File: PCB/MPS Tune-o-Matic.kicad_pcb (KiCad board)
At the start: 2 copper layers, 83.5 x 63 mm, 82 parts, among them J1 ISP, J2 MPS, J3 USB_B_Micro, J4 12V 1A IN (5.5/2.5), J5 12V IN, Q1 PZT2222A,115, Q2 PZT2222A,115, Q3 PZT2222A,115, Q4 PZT2222A,115, Q5 PZT2222A,115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

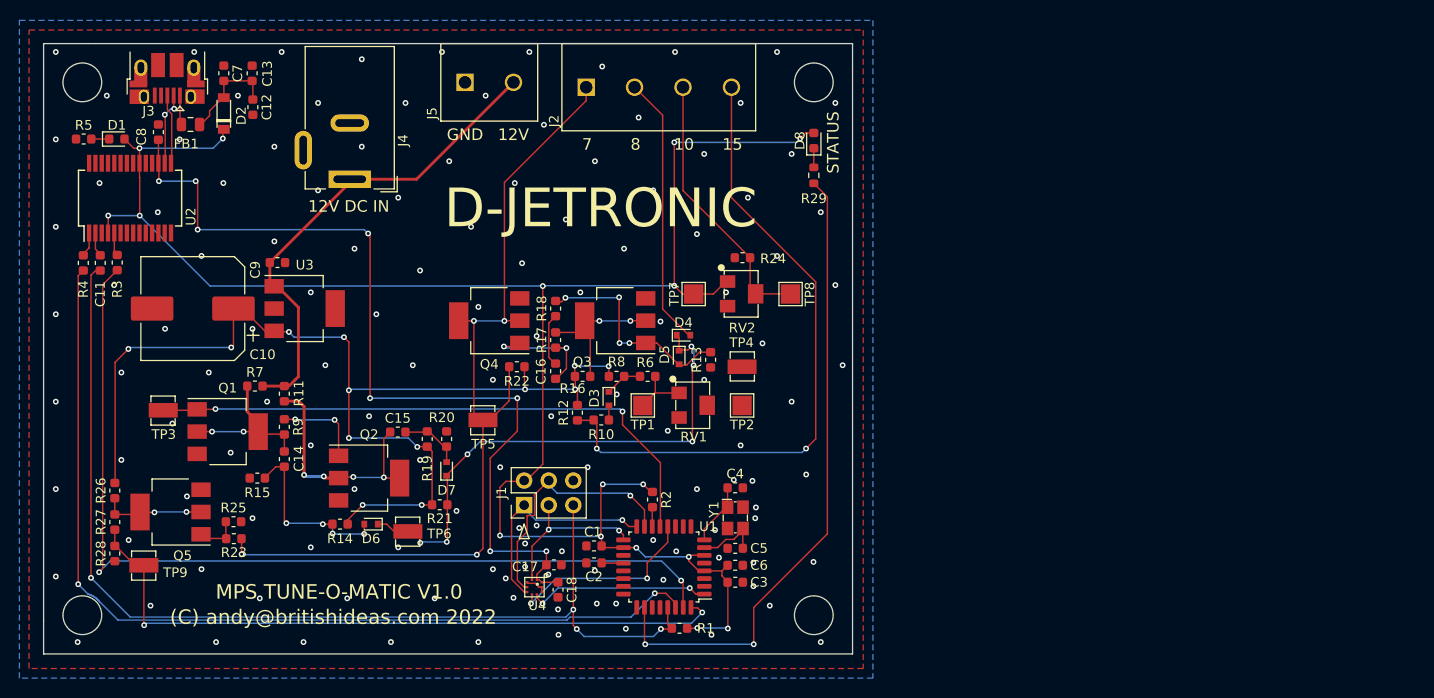
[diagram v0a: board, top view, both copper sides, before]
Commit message: Added LED for 12V power. Added resistor on MPS_STIMULUS signal. Moved track away from mounting hole. Fixed orientation of diodes. Added PDF of schematic. Updated manufacturing files.
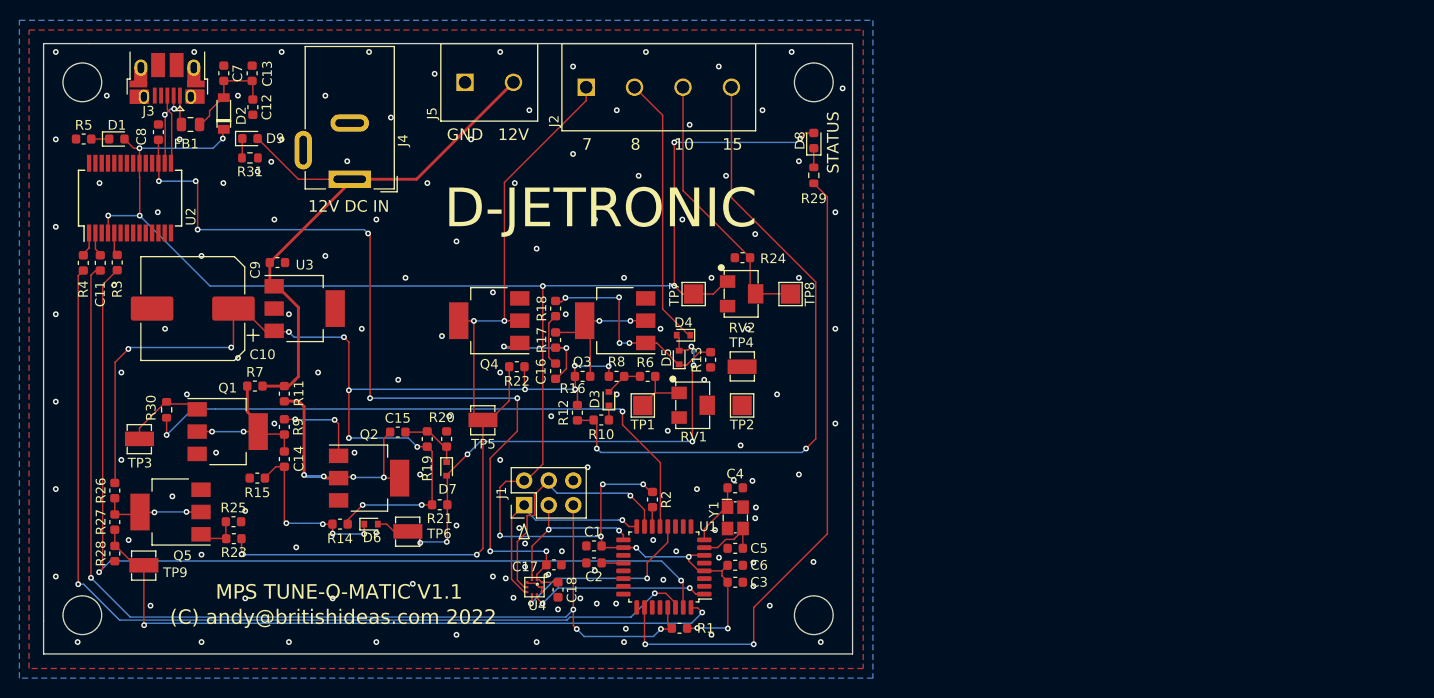
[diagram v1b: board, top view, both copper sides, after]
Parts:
- added D9: APT1608EC, LED_SMD:LED_0603_1608Metric, F.Cu at (70.8, 25.8)
- added R30: 10k, Resistor_SMD:R_0603_1608Metric, F.Cu at (62.2, 53.8)
- added R31: 510, Resistor_SMD:R_0603_1608Metric, F.Cu at (70.8, 27.8)
- C1: value 4.7uF e -> 4.7uF
- R1, R2, R3, R4: value 1K -> 1k
- moved TP3 3.83 mm to (59.4, 56.8)
- turned D3 to 90 degrees
- turned D4 to 180 degrees
- turned D5 to 90 degrees
- turned D6 to 0 degrees
- turned D7 to 270 degrees
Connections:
- D4 pad 1: /MPS Stimulator/EDGES -> /MPS-8
- D4 pad 2: /MPS-8 -> /MPS Stimulator/EDGES
- D5 pad 1: /MPS Stimulator/EDGES -> Net-(D5-Pad1)
- D5 pad 2: Net-(D5-Pad2) -> /MPS Stimulator/EDGES
- D6 pad 1: /MPS Stimulator/EDGES -> Net-(C14-Pad2)
- D6 pad 2: Net-(C14-Pad2) -> /MPS Stimulator/EDGES
- D7 pad 1: /MPS Stimulator/EDGES -> Net-(C15-Pad2)
- D7 pad 2: Net-(C15-Pad2) -> /MPS Stimulator/EDGES
- Q1 pad 1: /MPS_STIMULUS -> Net-(Q1-Pad1)
- Q3 pad 1: Net-(D5-Pad2) -> Net-(D5-Pad1)
- R10 pad 2: Net-(D3-Pad2) -> Net-(D3-Pad1)
- R13 pad 2: Net-(D5-Pad2) -> Net-(D5-Pad1)
- R18 pad 2: Net-(D5-Pad2) -> Net-(D5-Pad1)
- R6 pad 1: Net-(D3-Pad1) -> Net-(D3-Pad2)
- R8 pad 1: Net-(D3-Pad1) -> Net-(D3-Pad2)
- TP3 pad 1: /MPS_STIMULUS -> Net-(Q1-Pad1)
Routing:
- net Net-(D5-Pad2): track 22.3 -> 0.00 mm, vias 4 -> 0
- net Net-(D5-Pad1): track 0.00 -> 22.3 mm, vias 0 -> 4
- net +12V: track 49.9 -> 61.2 mm
- net Net-(Q1-Pad1): track 0.00 -> 8.69 mm
- net Net-(D3-Pad2): track 1.34 -> 3.71 mm
- net Net-(D3-Pad1): track 3.71 -> 1.34 mm
- net /MPS_STIMULUS: track 61.2 -> 63.5 mm
- net Net-(D9-Pad1): track 0.00 -> 2.02 mm
- net GND: vias 132 -> 134
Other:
- board text added: "MPS TUNE-O-MATIC V1.1"
- board text removed: "MPS TUNE-O-MATIC V1.0"

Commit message: Started work on V2.0 with vacuum monitoring.
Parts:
- added C19: 100nF, Capacitor_SMD:C_0603_1608Metric, F.Cu at (185.0, 64.0)
- added C20: 100nF, Capacitor_SMD:C_0603_1608Metric, F.Cu at (189.2, 61.0)
- added J6: GPIO, Britishideas:PhoenixContact_COMBICON_PT_4, F.Cu at (136.0, 20.5)
- added REF**: Pressure_Connector, Britishideas:Pressure_Connector, F.Cu at (144.0, 50.0)
- added U5: BMP390, Britishideas:LGA-2x2-10-pin, F.Cu at (188.6, 64.7)
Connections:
- U1 pad 10: (no net) -> Net-(J6-Pad2)
- U1 pad 11: (no net) -> /~CS_VAC_PRESSURE
- U1 pad 2: (no net) -> /INT_VAC_PRESSURE
- U1 pad 9: (no net) -> Net-(J6-Pad3)
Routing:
- net GND: vias 134 -> 23
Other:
- board size 83.5 x 63 mm -> 112.5 x 63 mm
- board text added: "(C) andy@britishideas.com 2023"
- board text added: "GPIO"
- board text added: "MPS TUNE-O-MATIC V2.0"
- board text removed: "(C) andy@britishideas.com 2022"
- board text removed: "MPS TUNE-O-MATIC V1.1"
